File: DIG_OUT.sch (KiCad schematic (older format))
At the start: 17 parts, among them Q5 BCP56, Q6 BCP56, Q7 BCP56, Q8 BCP56, U7 PC847

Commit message: Finished the schematic, except for maybe a couple test points.
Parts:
- removed U7: PC847, Package_DIP:DIP-16_W7.62mm, symbol Isolator:PC847
- added U9: ELQ3H7, Package_SO:SOP-16_3.9x9.9mm_P1.27mm, symbol Isolator:LTV-247
- Q5, Q6, Q7, Q8: footprint Package_TO_SOT_SMD:SOT-223-3_TabPin2 -> Package_TO_SOT_SMD:SOT-223
- renumbered R50 to R53, R51 to R54, R52 to R55, R53 to R56, R54 to R57, R55 to R58, R56 to R59, R57 to R60, R58 to R61, R59 to R62, R60 to R63, R61 to R64
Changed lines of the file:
@@
 AR Path="/60B28EA9/60CAAB2D" Ref="R?"  Part="1"
 AR Path="/60BBF151/60CAAB2D" Ref="R?"  Part="1"
-AR Path="/60BA9C29/60CAAB2D" Ref="R50"  Part="1"
-F 0 "R50" V 3655 3750 50  0000 C CNN
+AR Path="/60BA9C29/60CAAB2D" Ref="R53"  Part="1"
+F 0 "R53" V 3655 3750 50  0000 C CNN
 F 1 "470" V 3564 3750 50  0000 C CNN
 F 2 "Resistor_SMD:R_0805_2012Metric" V 3490 3740 50  0001 C CNN
@@
 AR Path="/60B28EA9/60CDED91" Ref="R?"  Part="1"
 AR Path="/60BBF151/60CDED91" Ref="R?"  Part="1"
-AR Path="/60BA9C29/60CDED91" Ref="R51"  Part="1"
-F 0 "R51" V 3655 5300 50  0000 C CNN
+AR Path="/60BA9C29/60CDED91" Ref="R54"  Part="1"
+F 0 "R54" V 3655 5300 50  0000 C CNN
 F 1 "470" V 3564 5300 50  0000 C CNN
 F 2 "Resistor_SMD:R_0805_2012Metric" V 3490 5290 50  0001 C CNN
@@
 AR Path="/60B28EA9/60CF8664" Ref="R?"  Part="1"
 AR Path="/60BBF151/60CF8664" Ref="R?"  Part="1"
-AR Path="/60BA9C29/60CF8664" Ref="R54"  Part="1"
-F 0 "R54" V 4600 4950 50  0000 C CNN
+AR Path="/60BA9C29/60CF8664" Ref="R57"  Part="1"
+F 0 "R57" V 4600 4950 50  0000 C CNN
 F 1 "2.2k" V 4500 4950 50  0000 C CNN
 F 2 "Resistor_SMD:R_0805_2012Metric" V 4740 4940 50  0001 C CNN
@@
 AR Path="/60B28EA9/60D022B0" Ref="R?"  Part="1"
 AR Path="/60BBF151/60D022B0" Ref="R?"  Part="1"
-AR Path="/60BA9C29/60D022B0" Ref="R55"  Part="1"
-F 0 "R55" V 4600 5300 50  0000 C CNN
+AR Path="/60BA9C29/60D022B0" Ref="R58"  Part="1"
+F 0 "R58" V 4600 5300 50  0000 C CNN
 F 1 "4.7k" V 4500 5300 50  0000 C CNN
 F 2 "Resistor_SMD:R_0805_2012Metric" V 4740 5290 50  0001 C CNN
@@
 AR Path="/60B28EA9/60B54B1B" Ref="R?"  Part="1"
 AR Path="/60BBF151/60B54B1B" Ref="R?"  Part="1"
-AR Path="/60BA9C29/60B54B1B" Ref="R52"  Part="1"
-F 0 "R52" V 4600 3400 50  0000 C CNN
+AR Path="/60BA9C29/60B54B1B" Ref="R55"  Part="1"
+F 0 "R55" V 4600 3400 50  0000 C CNN
 F 1 "2.2k" V 4500 3400 50  0000 C CNN
 F 2 "Resistor_SMD:R_0805_2012Metric" V 4740 3390 50  0001 C CNN
@@
 AR Path="/60B28EA9/60B54B27" Ref="R?"  Part="1"
 AR Path="/60BBF151/60B54B27" Ref="R?"  Part="1"
-AR Path="/60BA9C29/60B54B27" Ref="R53"  Part="1"
-F 0 "R53" V 4600 3750 50  0000 C CNN
+AR Path="/60BA9C29/60B54B27" Ref="R56"  Part="1"
+F 0 "R56" V 4600 3750 50  0000 C CNN
 F 1 "4.7k" V 4500 3750 50  0000 C CNN
 F 2 "Resistor_SMD:R_0805_2012Metric" V 4740 3740 50  0001 C CNN
@@
 AR Path="/60B28EA9/60F0DFB3" Ref="R?"  Part="1"
 AR Path="/60BBF151/60F0DFB3" Ref="R?"  Part="1"
-AR Path="/60BA9C29/60F0DFB3" Ref="R56"  Part="1"
-F 0 "R56" V 7155 3750 50  0000 C CNN
+AR Path="/60BA9C29/60F0DFB3" Ref="R59"  Part="1"
+F 0 "R59" V 7155 3750 50  0000 C CNN
 F 1 "470" V 7064 3750 50  0000 C CNN
 F 2 "Resistor_SMD:R_0805_2012Metric" V 6990 3740 50  0001 C CNN
@@
 AR Path="/60B28EA9/60F0DFC8" Ref="R?"  Part="1"
 AR Path="/60BBF151/60F0DFC8" Ref="R?"  Part="1"
-AR Path="/60BA9C29/60F0DFC8" Ref="R57"  Part="1"
-F 0 "R57" V 7155 5300 50  0000 C CNN
+AR Path="/60BA9C29/60F0DFC8" Ref="R60"  Part="1"
+F 0 "R60" V 7155 5300 50  0000 C CNN
 F 1 "470" V 7064 5300 50  0000 C CNN
 F 2 "Resistor_SMD:R_0805_2012Metric" V 6990 5290 50  0001 C CNN
@@
 AR Path="/60B28EA9/60F0DFD2" Ref="R?"  Part="1"
 AR Path="/60BBF151/60F0DFD2" Ref="R?"  Part="1"
-AR Path="/60BA9C29/60F0DFD2" Ref="R60"  Part="1"
-F 0 "R60" V 8100 4950 50  0000 C CNN
+AR Path="/60BA9C29/60F0DFD2" Ref="R63"  Part="1"
+F 0 "R63" V 8100 4950 50  0000 C CNN
 F 1 "2.2k" V 8000 4950 50  0000 C CNN
 F 2 "Resistor_SMD:R_0805_2012Metric" V 8240 4940 50  0001 C CNN
@@
 AR Path="/60B28EA9/60F0DFDE" Ref="R?"  Part="1"
 AR Path="/60BBF151/60F0DFDE" Ref="R?"  Part="1"
-AR Path="/60BA9C29/60F0DFDE" Ref="R61"  Part="1"
-F 0 "R61" V 8100 5300 50  0000 C CNN
+AR Path="/60BA9C29/60F0DFDE" Ref="R64"  Part="1"
+F 0 "R64" V 8100 5300 50  0000 C CNN
 F 1 "4.7k" V 8000 5300 50  0000 C CNN
 F 2 "Resistor_SMD:R_0805_2012Metric" V 8240 5290 50  0001 C CNN
@@
 AR Path="/60B28EA9/60F0DFF0" Ref="R?"  Part="1"
 AR Path="/60BBF151/60F0DFF0" Ref="R?"  Part="1"
-AR Path="/60BA9C29/60F0DFF0" Ref="R58"  Part="1"
-F 0 "R58" V 8100 3400 50  0000 C CNN
+AR Path="/60BA9C29/60F0DFF0" Ref="R61"  Part="1"
+F 0 "R61" V 8100 3400 50  0000 C CNN
 F 1 "2.2k" V 8000 3400 50  0000 C CNN
 F 2 "Resistor_SMD:R_0805_2012Metric" V 8240 3390 50  0001 C CNN
@@
 AR Path="/60B28EA9/60F0DFFC" Ref="R?"  Part="1"
 AR Path="/60BBF151/60F0DFFC" Ref="R?"  Part="1"
-AR Path="/60BA9C29/60F0DFFC" Ref="R59"  Part="1"
-F 0 "R59" V 8100 3750 50  0000 C CNN
+AR Path="/60BA9C29/60F0DFFC" Ref="R62"  Part="1"
+F 0 "R62" V 8100 3750 50  0000 C CNN
 F 1 "4.7k" V 8000 3750 50  0000 C CNN
 F 2 "Resistor_SMD:R_0805_2012Metric" V 8240 3740 50  0001 C CNN
@@
 Text GLabel 7800 3750 0    50   Input ~ 0
 GND
-$Comp
-L Isolator:PC847 U7
-U 1 1 60F682D9
-P 4150 3300
-F 0 "U7" H 4150 3625 50  0000 C CNN
-F 1 "PC847" H 4150 3534 50  0000 C CNN
-F 2 "Package_DIP:DIP-16_W7.62mm" H 3950 3100 50  0001 L CIN
-F 3 "http://www.soselectronic.cz/a_info/resource/d/pc817.pdf" H 4150 3300 50  0001 L CNN
-	1    4150 3300
-	1    0    0    -1
-$EndComp
-$Comp
-L Isolator:PC847 U7
-U 2 1 60F6906A
-P 4150 4850
-F 0 "U7" H 4150 5175 50  0000 C CNN
-F 1 "PC847" H 4150 5084 50  0000 C CNN
-F 2 "Package_DIP:DIP-16_W7.62mm" H 3950 4650 50  0001 L CIN
-F 3 "http://www.soselectronic.cz/a_info/resource/d/pc817.pdf" H 4150 4850 50  0001 L CNN
-	2    4150 4850
-	1    0    0    -1
-$EndComp
-$Comp
-L Isolator:PC847 U7
-U 3 1 60F69643
-P 7650 3300
-F 0 "U7" H 7650 3625 50  0000 C CNN
-F 1 "PC847" H 7650 3534 50  0000 C CNN
-F 2 "Package_DIP:DIP-16_W7.62mm" H 7450 3100 50  0001 L CIN
-F 3 "http://www.soselectronic.cz/a_info/resource/d/pc817.pdf" H 7650 3300 50  0001 L CNN
-	3    7650 3300
-	1    0    0    -1
-$EndComp
-$Comp
-L Isolator:PC847 U7
-U 4 1 60F6A699
-P 7650 4850
-F 0 "U7" H 7650 5175 50  0000 C CNN
-F 1 "PC847" H 7650 5084 50  0000 C CNN
-F 2 "Package_DIP:DIP-16_W7.62mm" H 7450 4650 50  0001 L CIN
-F 3 "http://www.soselectronic.cz/a_info/resource/d/pc817.pdf" H 7650 4850 50  0001 L CNN
-	4    7650 4850
-	1    0    0    -1
-$EndComp
 Wire Wire Line
 	3050 2850 3850 2850
@@
 F 0 "Q7" H 8841 3446 50  0000 L CNN
 F 1 "BCP56" H 8841 3355 50  0000 L CNN
-F 2 "Package_TO_SOT_SMD:SOT-223-3_TabPin2" H 8850 3325 50  0001 L CIN
+F 2 "Package_TO_SOT_SMD:SOT-223" H 8850 3325 50  0001 L CIN
 F 3 "http://cache.nxp.com/documents/data_sheet/BCP56_BCX56_BC56PA.pdf?pspll=1" H 8650 3400 50  0001 L CNN
 	1    8650 3400
@@
 F 0 "Q8" H 8841 4996 50  0000 L CNN
 F 1 "BCP56" H 8841 4905 50  0000 L CNN
-F 2 "Package_TO_SOT_SMD:SOT-223-3_TabPin2" H 8850 4875 50  0001 L CIN
+F 2 "Package_TO_SOT_SMD:SOT-223" H 8850 4875 50  0001 L CIN
 F 3 "http://cache.nxp.com/documents/data_sheet/BCP56_BCX56_BC56PA.pdf?pspll=1" H 8650 4950 50  0001 L CNN
 	1    8650 4950
@@
 F 0 "Q5" H 5341 3446 50  0000 L CNN
 F 1 "BCP56" H 5341 3355 50  0000 L CNN
-F 2 "Package_TO_SOT_SMD:SOT-223-3_TabPin2" H 5350 3325 50  0001 L CIN
+F 2 "Package_TO_SOT_SMD:SOT-223" H 5350 3325 50  0001 L CIN
 F 3 "http://cache.nxp.com/documents/data_sheet/BCP56_BCX56_BC56PA.pdf?pspll=1" H 5150 3400 50  0001 L CNN
 	1    5150 3400
@@
 F 0 "Q6" H 5341 4996 50  0000 L CNN
 F 1 "BCP56" H 5341 4905 50  0000 L CNN
-F 2 "Package_TO_SOT_SMD:SOT-223-3_TabPin2" H 5350 4875 50  0001 L CIN
+F 2 "Package_TO_SOT_SMD:SOT-223" H 5350 4875 50  0001 L CIN
 F 3 "http://cache.nxp.com/documents/data_sheet/BCP56_BCX56_BC56PA.pdf?pspll=1" H 5150 4950 50  0001 L CNN
 	1    5150 4950
 	1    0    0    -1
 $EndComp
+$Comp
+L Isolator:LTV-247 U9
+U 1 1 61E80CC7
+P 4150 3300
+F 0 "U9" H 4150 3625 50  0000 C CNN
+F 1 "ELQ3H7" H 4150 3534 50  0000 C CNN
+F 2 "Package_SO:SOP-16_3.9x9.9mm_P1.27mm" H 3950 3100 50  0001 L CIN
+F 3 "http://optoelectronics.liteon.com/upload/download/DS70-2009-0014/LTV-2X7%20sereis%20Mar17.PDF" H 4150 3300 50  0001 L CNN
+	1    4150 3300
+	1    0    0    -1
+$EndComp
+$Comp
+L Isolator:LTV-247 U9
+U 2 1 61E8602A
+P 4150 4850
+F 0 "U9" H 4150 5175 50  0000 C CNN
+F 1 "ELQ3H7" H 4150 5084 50  0000 C CNN
+F 2 "Package_SO:SOP-16_3.9x9.9mm_P1.27mm" H 3950 4650 50  0001 L CIN
+F 3 "http://optoelectronics.liteon.com/upload/download/DS70-2009-0014/LTV-2X7%20sereis%20Mar17.PDF" H 4150 4850 50  0001 L CNN
+	2    4150 4850
+	1    0    0    -1
+$EndComp
+$Comp
+L Isolator:LTV-247 U9
+U 3 1 61E86ED5
+P 7650 3300
+F 0 "U9" H 7650 3625 50  0000 C CNN
+F 1 "ELQ3H7" H 7650 3534 50  0000 C CNN
+F 2 "Package_SO:SOP-16_3.9x9.9mm_P1.27mm" H 7450 3100 50  0001 L CIN
+F 3 "http://optoelectronics.liteon.com/upload/download/DS70-2009-0014/LTV-2X7%20sereis%20Mar17.PDF" H 7650 3300 50  0001 L CNN
+	3    7650 3300
+	1    0    0    -1
+$EndComp
+$Comp
+L Isolator:LTV-247 U9
+U 4 1 61E87B1B
+P 7650 4850
+F 0 "U9" H 7650 5175 50  0000 C CNN
+F 1 "ELQ3H7" H 7650 5084 50  0000 C CNN
+F 2 "Package_SO:SOP-16_3.9x9.9mm_P1.27mm" H 7450 4650 50  0001 L CIN
+F 3 "http://optoelectronics.liteon.com/upload/download/DS70-2009-0014/LTV-2X7%20sereis%20Mar17.PDF" H 7650 4850 50  0001 L CNN
+	4    7650 4850
+	1    0    0    -1
+$EndComp

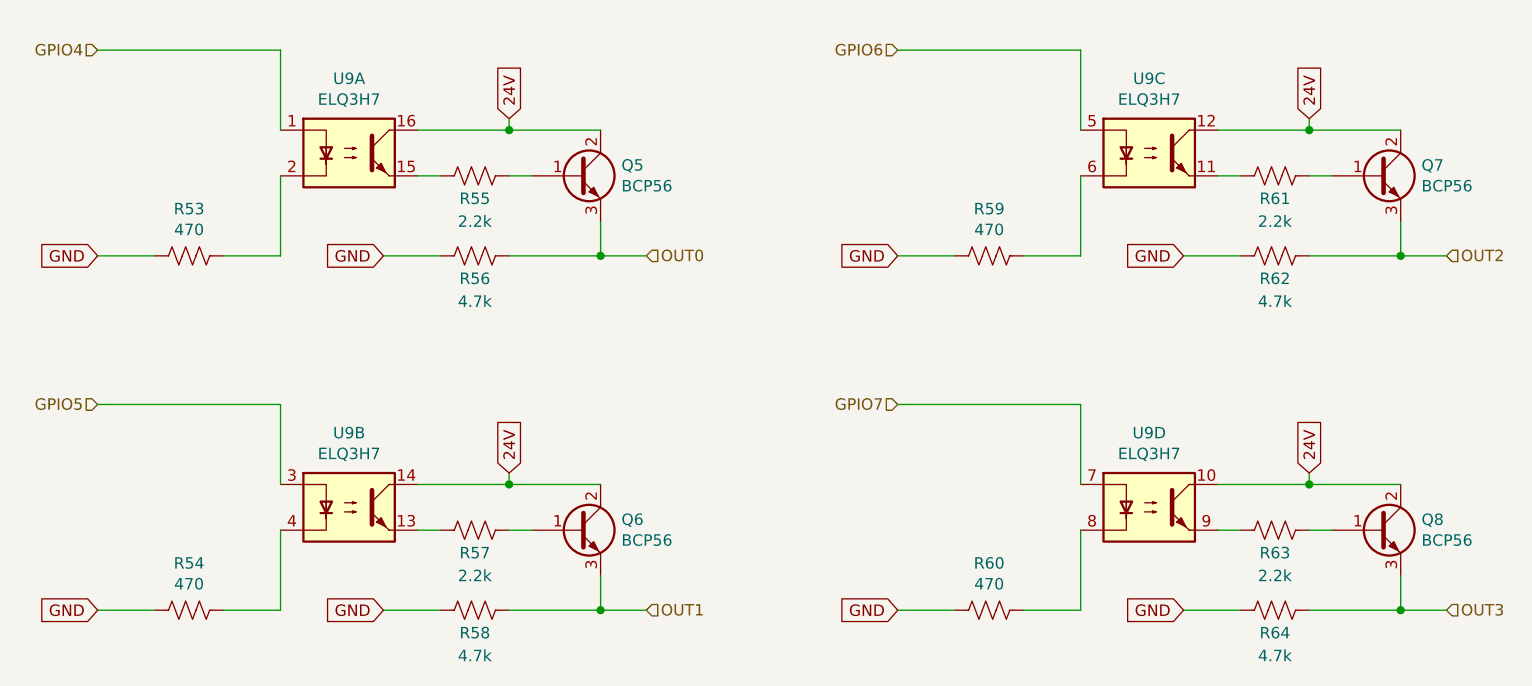
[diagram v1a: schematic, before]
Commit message: Everything but the 24V output is routed
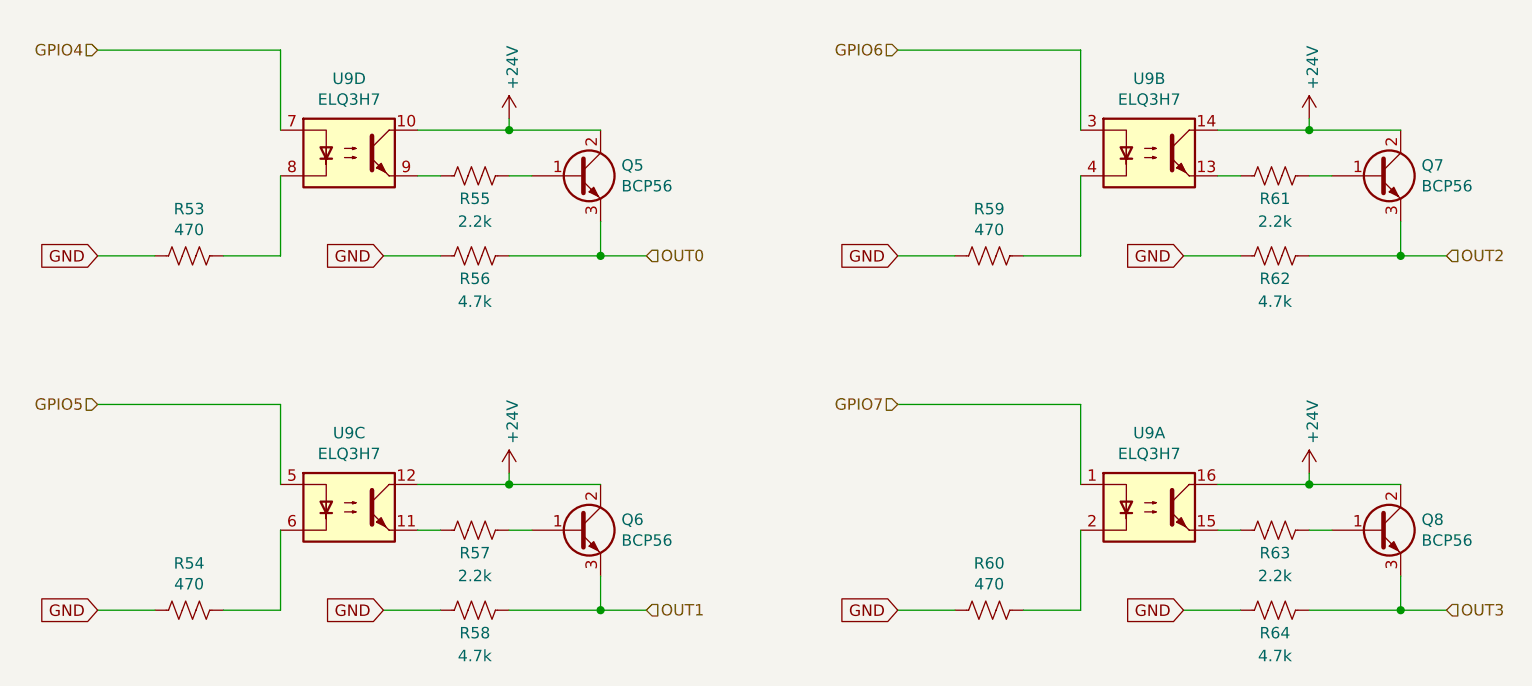
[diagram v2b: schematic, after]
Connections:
- net GPIO4: now also U9.7; no longer U9.1
- net GPIO5: now also U9.5; no longer U9.3
- net GPIO6: now also U9.3; no longer U9.5
- net GPIO7: now also U9.1; no longer U9.7
- net at R55.1: now also U9.9; no longer U9.15
- net at R53.2: now also U9.8; no longer U9.2
- net at R54.2: now also U9.6; no longer U9.4
- net at R57.1: now also U9.11; no longer U9.13
- net at R59.2: now also U9.4; no longer U9.6
- net at R60.2: now also U9.2; no longer U9.8
- net at R63.1: now also U9.15; no longer U9.9
- net at R61.1: now also U9.13; no longer U9.11
- net 24V renamed +24V
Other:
- moved on the sheet: U9A, U9B, U9C, U9D
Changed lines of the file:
@@
 Text GLabel 3050 5300 0    50   Input ~ 0
 GND
-Text GLabel 4850 4700 1    50   Input ~ 0
-24V
 Text HLabel 5450 5300 2    50   Input ~ 0
 OUT1
@@
 	5250 5300 5450 5300
 Connection ~ 5250 5300
-Text GLabel 4850 3150 1    50   Input ~ 0
-24V
 $Comp
 L Device:R_US R?
@@
 Text GLabel 6550 5300 0    50   Input ~ 0
 GND
-Text GLabel 8350 4700 1    50   Input ~ 0
-24V
 Text HLabel 8950 5300 2    50   Input ~ 0
 OUT3
@@
 	8750 5300 8950 5300
 Connection ~ 8750 5300
-Text GLabel 8350 3150 1    50   Input ~ 0
-24V
 $Comp
 L Device:R_US R?
@@
 L Isolator:LTV-247 U9
 U 1 1 61E80CC7
+P 7650 4850
+F 0 "U9" H 7650 5175 50  0000 C CNN
+F 1 "ELQ3H7" H 7650 5084 50  0000 C CNN
+F 2 "Package_SO:SOP-16_3.9x9.9mm_P1.27mm" H 7450 4650 50  0001 L CIN
+F 3 "http://optoelectronics.liteon.com/upload/download/DS70-2009-0014/LTV-2X7%20sereis%20Mar17.PDF" H 7650 4850 50  0001 L CNN
+	1    7650 4850
+	1    0    0    -1
+$EndComp
+$Comp
+L Isolator:LTV-247 U9
+U 2 1 61E8602A
+P 7650 3300
+F 0 "U9" H 7650 3625 50  0000 C CNN
+F 1 "ELQ3H7" H 7650 3534 50  0000 C CNN
+F 2 "Package_SO:SOP-16_3.9x9.9mm_P1.27mm" H 7450 3100 50  0001 L CIN
+F 3 "http://optoelectronics.liteon.com/upload/download/DS70-2009-0014/LTV-2X7%20sereis%20Mar17.PDF" H 7650 3300 50  0001 L CNN
+	2    7650 3300
+	1    0    0    -1
+$EndComp
+$Comp
+L Isolator:LTV-247 U9
+U 3 1 61E86ED5
+P 4150 4850
+F 0 "U9" H 4150 5175 50  0000 C CNN
+F 1 "ELQ3H7" H 4150 5084 50  0000 C CNN
+F 2 "Package_SO:SOP-16_3.9x9.9mm_P1.27mm" H 3950 4650 50  0001 L CIN
+F 3 "http://optoelectronics.liteon.com/upload/download/DS70-2009-0014/LTV-2X7%20sereis%20Mar17.PDF" H 4150 4850 50  0001 L CNN
+	3    4150 4850
+	1    0    0    -1
+$EndComp
+$Comp
+L Isolator:LTV-247 U9
+U 4 1 61E87B1B
 P 4150 3300
 F 0 "U9" H 4150 3625 50  0000 C CNN
@@
 F 2 "Package_SO:SOP-16_3.9x9.9mm_P1.27mm" H 3950 3100 50  0001 L CIN
 F 3 "http://optoelectronics.liteon.com/upload/download/DS70-2009-0014/LTV-2X7%20sereis%20Mar17.PDF" H 4150 3300 50  0001 L CNN
-	1    4150 3300
-	1    0    0    -1
-$EndComp
-$Comp
-L Isolator:LTV-247 U9
-U 2 1 61E8602A
-P 4150 4850
-F 0 "U9" H 4150 5175 50  0000 C CNN
-F 1 "ELQ3H7" H 4150 5084 50  0000 C CNN
-F 2 "Package_SO:SOP-16_3.9x9.9mm_P1.27mm" H 3950 4650 50  0001 L CIN
-F 3 "http://optoelectronics.liteon.com/upload/download/DS70-2009-0014/LTV-2X7%20sereis%20Mar17.PDF" H 4150 4850 50  0001 L CNN
-	2    4150 4850
-	1    0    0    -1
-$EndComp
-$Comp
-L Isolator:LTV-247 U9
-U 3 1 61E86ED5
-P 7650 3300
-F 0 "U9" H 7650 3625 50  0000 C CNN
-F 1 "ELQ3H7" H 7650 3534 50  0000 C CNN
-F 2 "Package_SO:SOP-16_3.9x9.9mm_P1.27mm" H 7450 3100 50  0001 L CIN
-F 3 "http://optoelectronics.liteon.com/upload/download/DS70-2009-0014/LTV-2X7%20sereis%20Mar17.PDF" H 7650 3300 50  0001 L CNN
-	3    7650 3300
-	1    0    0    -1
-$EndComp
-$Comp
-L Isolator:LTV-247 U9
-U 4 1 61E87B1B
-P 7650 4850
-F 0 "U9" H 7650 5175 50  0000 C CNN
-F 1 "ELQ3H7" H 7650 5084 50  0000 C CNN
-F 2 "Package_SO:SOP-16_3.9x9.9mm_P1.27mm" H 7450 4650 50  0001 L CIN
-F 3 "http://optoelectronics.liteon.com/upload/download/DS70-2009-0014/LTV-2X7%20sereis%20Mar17.PDF" H 7650 4850 50  0001 L CNN
-	4    7650 4850
-	1    0    0    -1
-$EndComp
+	4    4150 3300
+	1    0    0    -1
+$EndComp
+$Comp
+L power:+24V #PWR?
+U 1 1 61E3EA42
+P 4850 3150
+AR Path="/61E3EA42" Ref="#PWR?"  Part="1"
+AR Path="/60BA9C29/61E3EA42" Ref="#PWR0101"  Part="1"
+F 0 "#PWR0101" H 4850 3000 50  0001 C CNN
+F 1 "+24V" V 4865 3278 50  0000 L CNN
+F 2 "" H 4850 3150 50  0001 C CNN
+F 3 "" H 4850 3150 50  0001 C CNN
+	1    4850 3150
+	1    0    0    -1
+$EndComp
+$Comp
+L power:+24V #PWR?
+U 1 1 61E3F9B2
+P 4850 4700
+AR Path="/61E3F9B2" Ref="#PWR?"  Part="1"
+AR Path="/60BA9C29/61E3F9B2" Ref="#PWR0102"  Part="1"
+F 0 "#PWR0102" H 4850 4550 50  0001 C CNN
+F 1 "+24V" V 4865 4828 50  0000 L CNN
+F 2 "" H 4850 4700 50  0001 C CNN
+F 3 "" H 4850 4700 50  0001 C CNN
+	1    4850 4700
+	1    0    0    -1
+$EndComp
+$Comp
+L power:+24V #PWR?
+U 1 1 61E40C60
+P 8350 3150
+AR Path="/61E40C60" Ref="#PWR?"  Part="1"
+AR Path="/60BA9C29/61E40C60" Ref="#PWR0103"  Part="1"
+F 0 "#PWR0103" H 8350 3000 50  0001 C CNN
+F 1 "+24V" V 8365 3278 50  0000 L CNN
+F 2 "" H 8350 3150 50  0001 C CNN
+F 3 "" H 8350 3150 50  0001 C CNN
+	1    8350 3150
+	1    0    0    -1
+$EndComp
+$Comp
+L power:+24V #PWR?
+U 1 1 61E41ADB
+P 8350 4700
+AR Path="/61E41ADB" Ref="#PWR?"  Part="1"
+AR Path="/60BA9C29/61E41ADB" Ref="#PWR0104"  Part="1"
+F 0 "#PWR0104" H 8350 4550 50  0001 C CNN
+F 1 "+24V" V 8365 4828 50  0000 L CNN
+F 2 "" H 8350 4700 50  0001 C CNN
+F 3 "" H 8350 4700 50  0001 C CNN
+	1    8350 4700
+	1    0    0    -1
+$EndComp
